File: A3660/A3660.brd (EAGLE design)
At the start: 207 x 98 mm, 130 parts, among them CN100 KEL8817-200-170S-F, J400 1X3PIN, U100 OSCILLATOR, U101 74F1803, U102 MC68040/68060, U103 DELAYLINE, U104 7407, U105 74F04, U200 74FCT373ASO, U201 74FCT374ASO, U202 74F32, U203 GAL16V8, U204 GAL22V10, U205 GAL22V10, U206 74F139, U207 GAL22V10, U208 GAL16V8, U209 GAL22V10, U211 GAL22V10, U212 74F257, U213 GAL22V10, U214 74FCT543A, U215 74FCT543A, U216 74FCT543A, U217 74FCT543A, U218 74FCT543A, U219 74FCT543A, U220 74FCT543A, U221 74FCT543A, U222 74FCT543A, U400 GAL22V10, U401 GAL16V8, U402 74FCT244A, U500 74F257

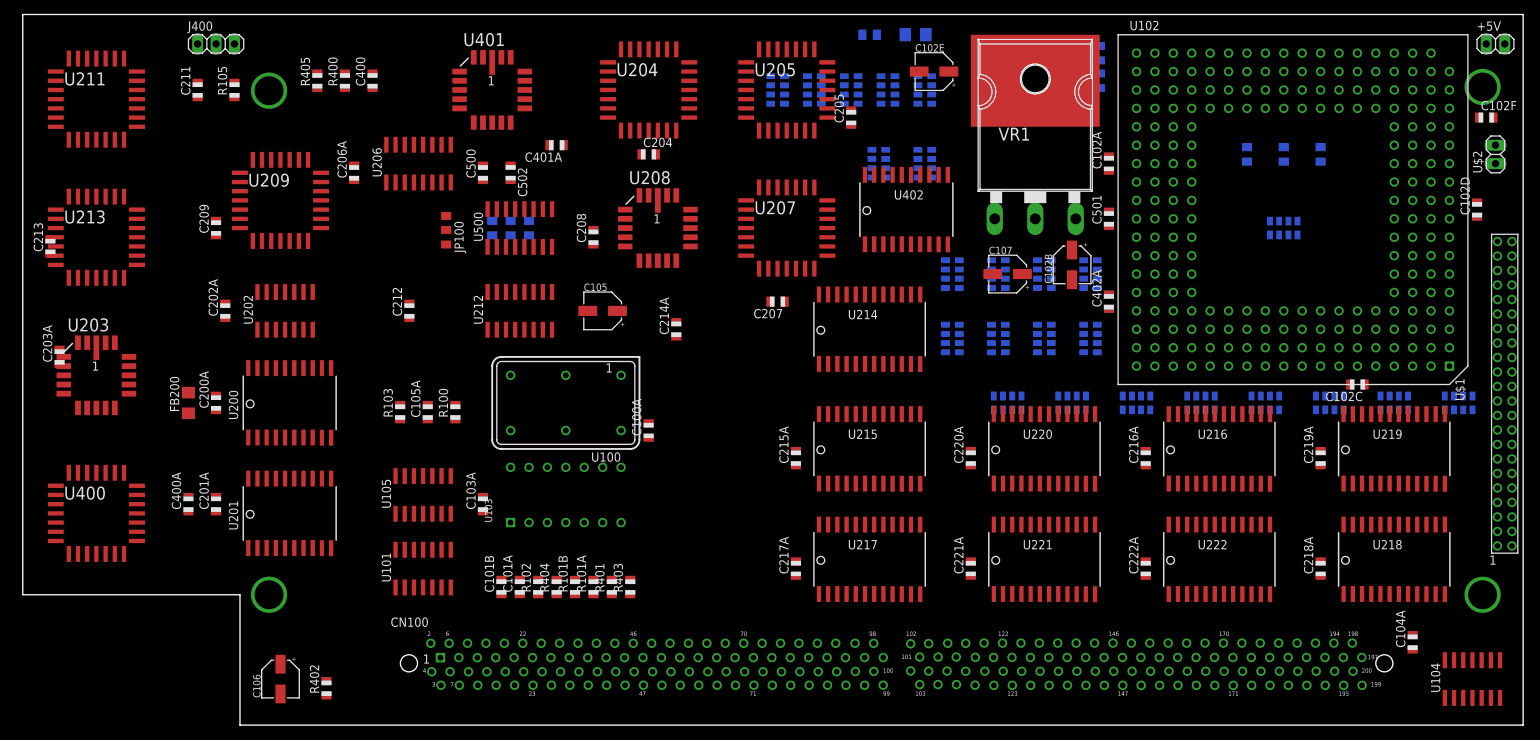
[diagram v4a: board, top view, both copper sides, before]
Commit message: Datalines routed,,  most addresslines aswell
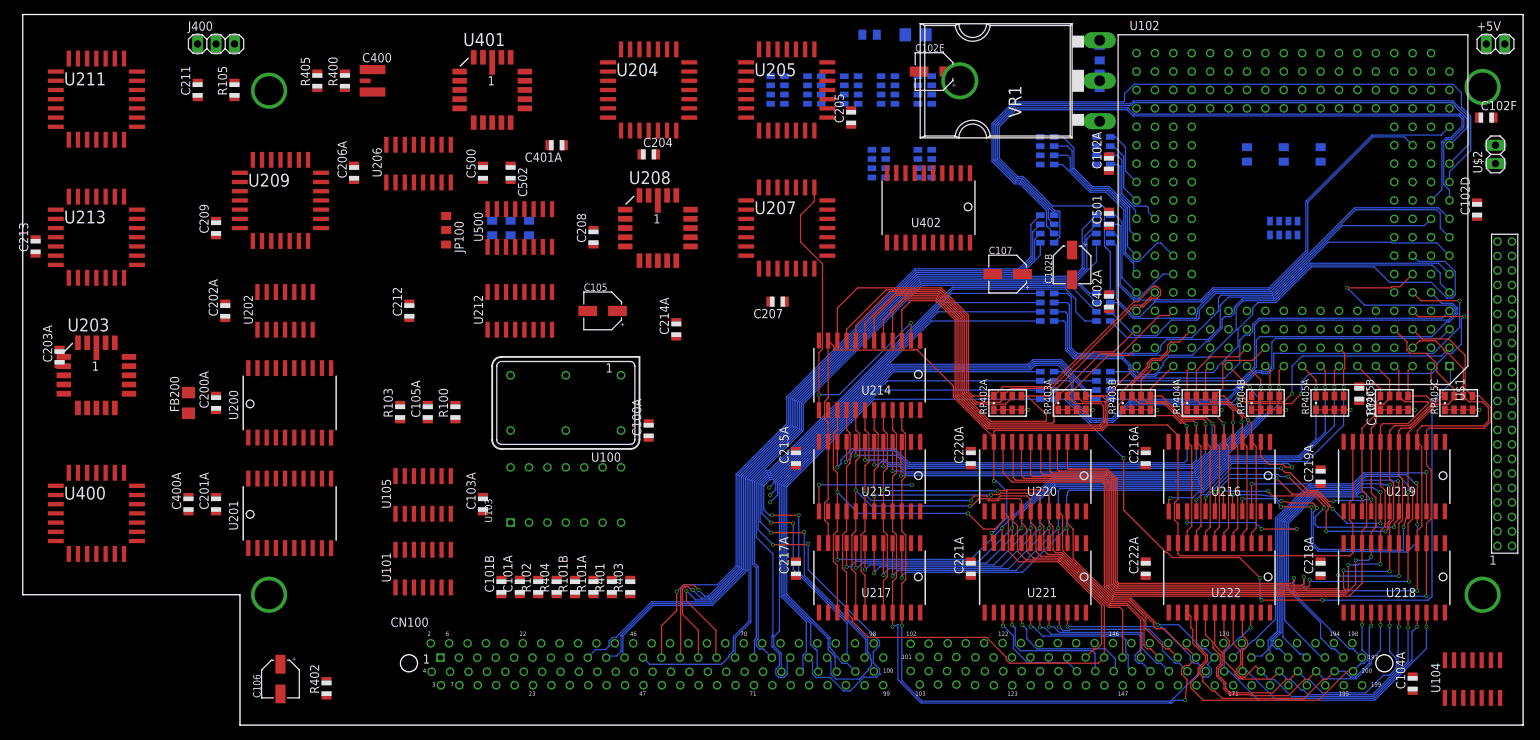
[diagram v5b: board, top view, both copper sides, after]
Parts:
- C400: value 100nF -> RH5VA43A; device A3660:R0805 -> A3660:RH5VA43A
- R400: value 100 -> 10K
- moved RP402A 62.2 mm to (135.9, 44.5), flipped to the top
- moved RP405C 62.2 mm to (198.1, 44.5), flipped to the top
- moved RP403A 44.4 mm to (144.8, 44.5), flipped to the top
- moved RP405B 44.4 mm to (189.2, 44.5), flipped to the top
- moved RP108 26.9 mm to (149.1, 79.2), turned to 90 degrees
- moved RP403B 26.7 mm to (153.7, 44.5), flipped to the top
- moved RP405A 26.7 mm to (180.3, 44.5), flipped to the top
- moved RP104 21.3 mm to (149.1, 57.7), turned to 90 degrees
- moved RP107 18.3 mm to (141.4, 79.2), turned to 90 degrees
- moved RP102 10.4 mm to (149.1, 46.9), turned to 90 degrees
- moved RP106 10.2 mm to (149.1, 68.5), turned to 90 degrees
- moved RP404A 8.89 mm to (162.6, 44.5), flipped to the top
- moved RP404B 8.89 mm to (171.4, 44.5), flipped to the top
- moved RP101 8.81 mm to (141.4, 46.9), turned to 90 degrees
- moved RP105 8.62 mm to (141.4, 68.5), turned to 90 degrees
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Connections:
- net +5V: now also C400.2
- net GND: now also C400.3, U100.4; no longer C400.1
- net N$1: now also C400.1; no longer C400.2
- net N$6: now also U100.11
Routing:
- net R_W060: track 0.00 -> 159.6 mm, vias 0 -> 2
- net 060D0: track 0.00 -> 123.5 mm, vias 0 -> 2
- net 060D1: track 0.00 -> 123.0 mm, vias 0 -> 2
- net D24: track 0.00 -> 119.2 mm, vias 0 -> 2
- net D25: track 0.00 -> 118.2 mm, vias 0 -> 2
- net 060D2: track 0.00 -> 113.2 mm, vias 0 -> 2
- net 060A16: track 0.00 -> 112.6 mm
- net 060D5: track 0.00 -> 109.3 mm, vias 0 -> 2
- net A8: track 0.00 -> 108.6 mm
- net 060D4: track 0.00 -> 107.5 mm, vias 0 -> 2
- net A9: track 0.00 -> 105.9 mm
- net 060D3: track 0.00 -> 104.2 mm, vias 0 -> 2
- net A11: track 0.00 -> 103.4 mm
- net A10: track 0.00 -> 103.4 mm
- net 060D23: track 0.00 -> 103.0 mm, vias 0 -> 2
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- added copper zone on layer 15, net +3V3
- added copper zone on layer 15, net +5V
- added copper zone on layer 2, net GND

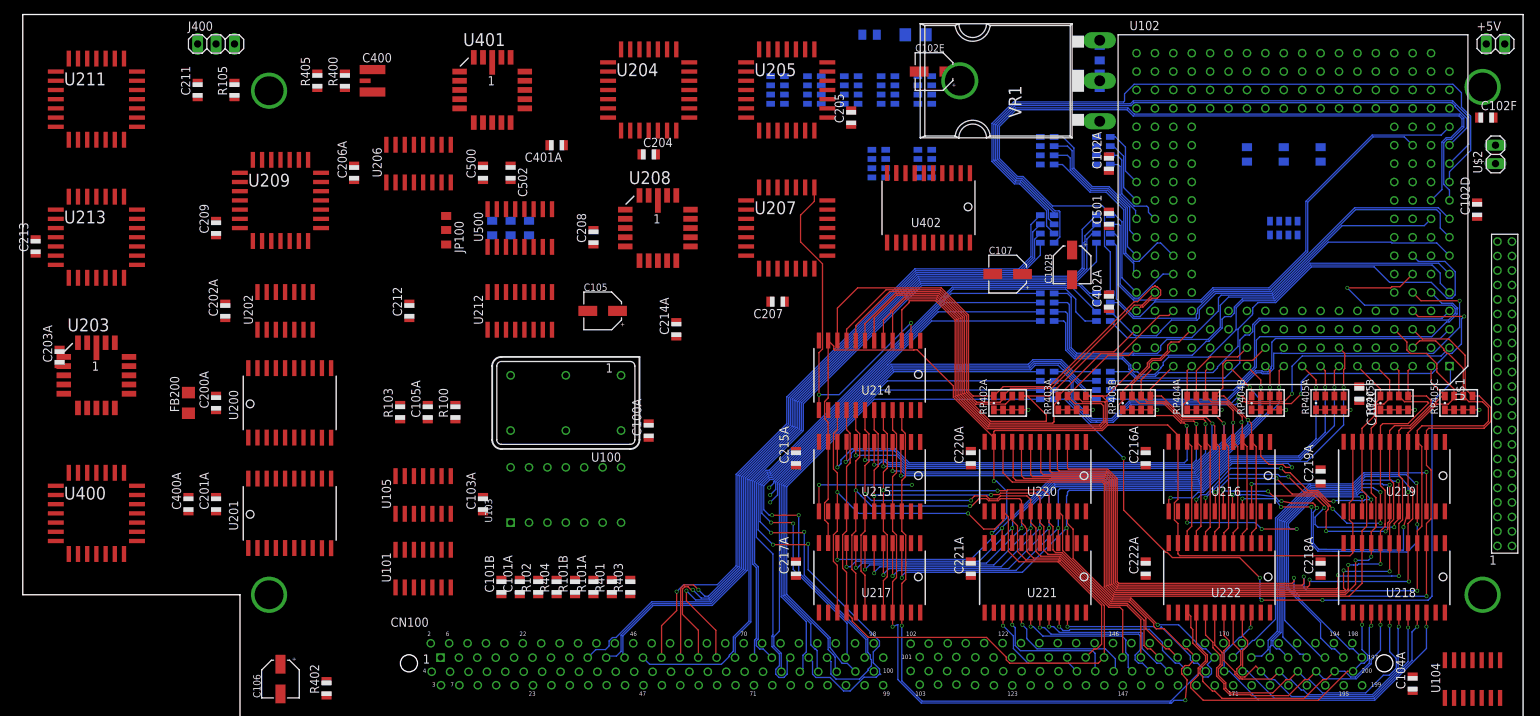
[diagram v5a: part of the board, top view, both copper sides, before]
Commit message: Addresssignals complete, IPL etc working on
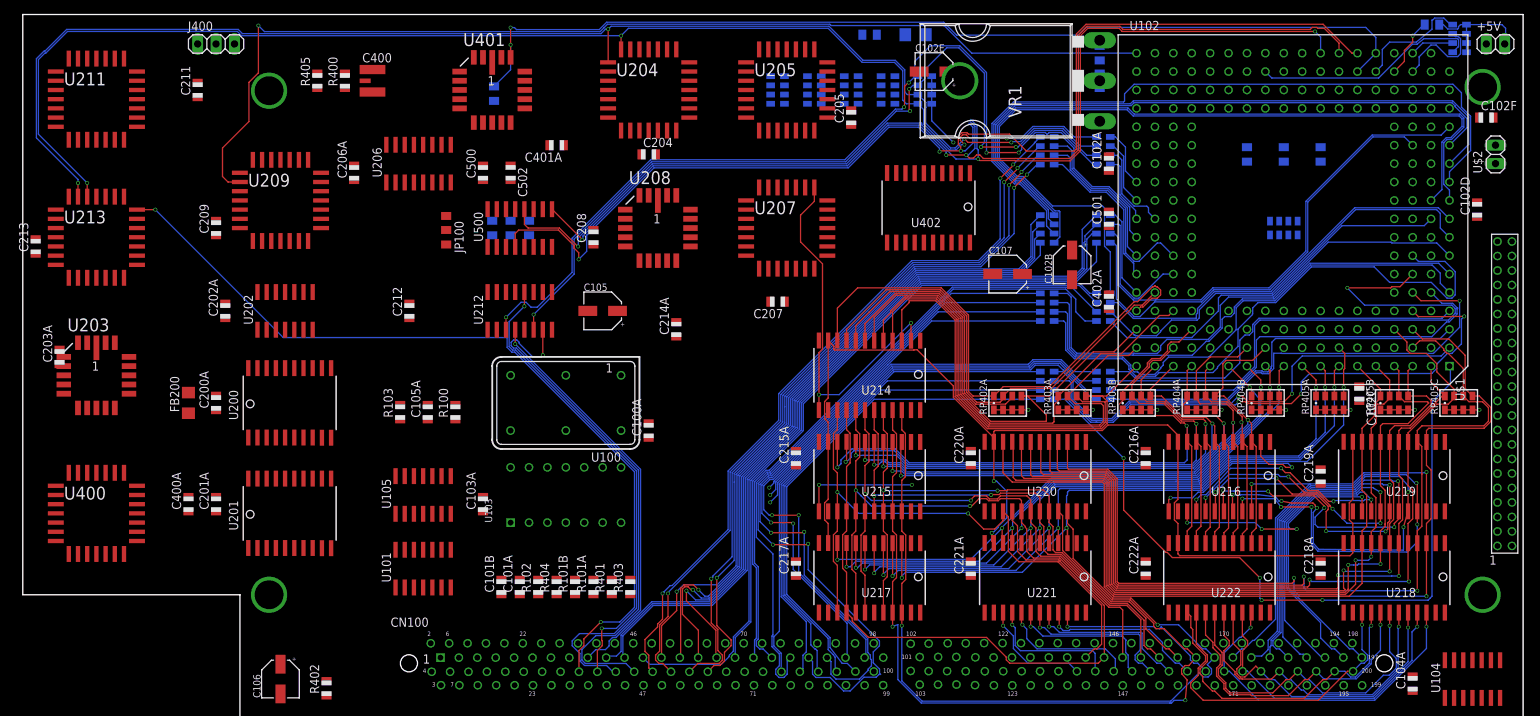
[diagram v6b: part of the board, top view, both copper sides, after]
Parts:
- removed RP100B: 1K, A3660:RP743-8
- added R100A: 1k, A3660:R0805
- moved RP100A 75.8 mm to (198.2, 94.7)
- moved R105 35.8 mm to (65.0, 87.1), flipped to the bottom, turned to 270 degrees
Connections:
- removed net N$10: RP100B.8
- removed net N$8: RP100B.6
- removed net N$9: RP100B.7
- net GND: now also R100A.1; no longer RP100B.1, RP100B.2, RP100B.3, RP100B.4
- net TCK: now also R100A.2; no longer RP100B.5
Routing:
- net A1: track 0.00 -> 187.6 mm, vias 0 -> 4
- net A0: track 0.00 -> 186.1 mm, vias 0 -> 4
- net _060IPL2: track 0.00 -> 158.3 mm, vias 0 -> 3
- net _BR060: track 0.00 -> 149.2 mm, vias 0 -> 1
- net _060IPL0: track 0.00 -> 148.7 mm, vias 0 -> 3
- net _060IPL1: track 0.00 -> 144.7 mm, vias 0 -> 3
- net _060EMUL: track 0.00 -> 138.4 mm, vias 0 -> 2
- net A3: track 0.00 -> 121.5 mm, vias 0 -> 5
- net 030A0: track 0.00 -> 116.7 mm, vias 0 -> 2
- net A2: track 0.00 -> 115.2 mm, vias 0 -> 5
- net A4: track 0.00 -> 102.4 mm, vias 0 -> 3
- net A5: track 0.00 -> 101.2 mm, vias 0 -> 3
- net A6: track 0.00 -> 99.9 mm, vias 0 -> 3
- net A7: track 0.00 -> 96.7 mm, vias 0 -> 3
- net 030A2: track 0.00 -> 73.2 mm, vias 0 -> 1
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
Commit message: Autoroute done
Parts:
- moved R108 55.7 mm to (93.1, 93.7), turned to 180 degrees
- moved R107 49.2 mm to (99.4, 93.6), turned to 180 degrees
- moved FB100 24.1 mm to (103.6, 81.3)
- moved R104 23.1 mm to (98.5, 81.2)
- moved C102C 22.1 mm to (168.3, 60.9), turned to 0 degrees
- moved C102F 17.0 mm to (185.4, 79.8), turned to 270 degrees
- moved C102D 15.9 mm to (185.2, 67.7)
- moved C102E 8.23 mm to (119.1, 95.0)
- moved C203A 3.05 mm to (2.03, 50.7)
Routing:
- net GND: track 16.0 -> 635.7 mm, vias 0 -> 19
- net BCLK: track 0.00 -> 386.0 mm, vias 0 -> 6
- net +5V: track 48.5 -> 410.0 mm, vias 9 -> 42
- net TT0: track 0.00 -> 308.0 mm, vias 0 -> 5
- net _060RSTI: track 0.00 -> 296.4 mm, vias 0 -> 12
- net _BGACK060: track 0.00 -> 288.9 mm, vias 0 -> 12
- net R_W060: track 159.6 -> 441.3 mm, vias 2 -> 9
- net _TEA: track 0.00 -> 243.8 mm, vias 0 -> 3
- net _R_W060: track 0.00 -> 240.0 mm, vias 0 -> 8
- net TT1: track 0.00 -> 219.5 mm, vias 0 -> 7
- net _AS060: track 0.00 -> 211.3 mm, vias 0 -> 9
- net TM2: track 0.00 -> 209.2 mm, vias 0 -> 5
- net _PLSTERM: track 0.00 -> 207.7 mm, vias 0 -> 6
- net TM1: track 0.00 -> 204.0 mm, vias 0 -> 5
- net TM0: track 0.00 -> 201.9 mm, vias 0 -> 10
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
